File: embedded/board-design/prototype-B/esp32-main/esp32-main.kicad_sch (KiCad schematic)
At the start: 30 parts, among them J1 Conn_ARM_JTAG_SWD_10, J2 Conn_01x08_Socket, J3 Conn_01x08_Socket, Q1 BC817, Q2 BC817, U1 ESP32-WROVER-E, U2 BD48ExxG

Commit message: [prototype-B]
Updated prototype-B README.md. Refactored schematic.

Signed-off-by: Nicolae-Andrei Vasile <vasilenicolaeandrei@gmail.com>
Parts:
- added D1: SMD22WS-TP, Diode_SMD:D_SOD-323_HandSoldering, symbol Device:D_Schottky
- renumbered D1 to D2
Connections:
- net +3V3: now also D1.1 (K); no longer J1.1 (VTref)
- new net: D1.2 (A), J1.1 (VTref)
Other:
- moved on the sheet: R1, R2, R3

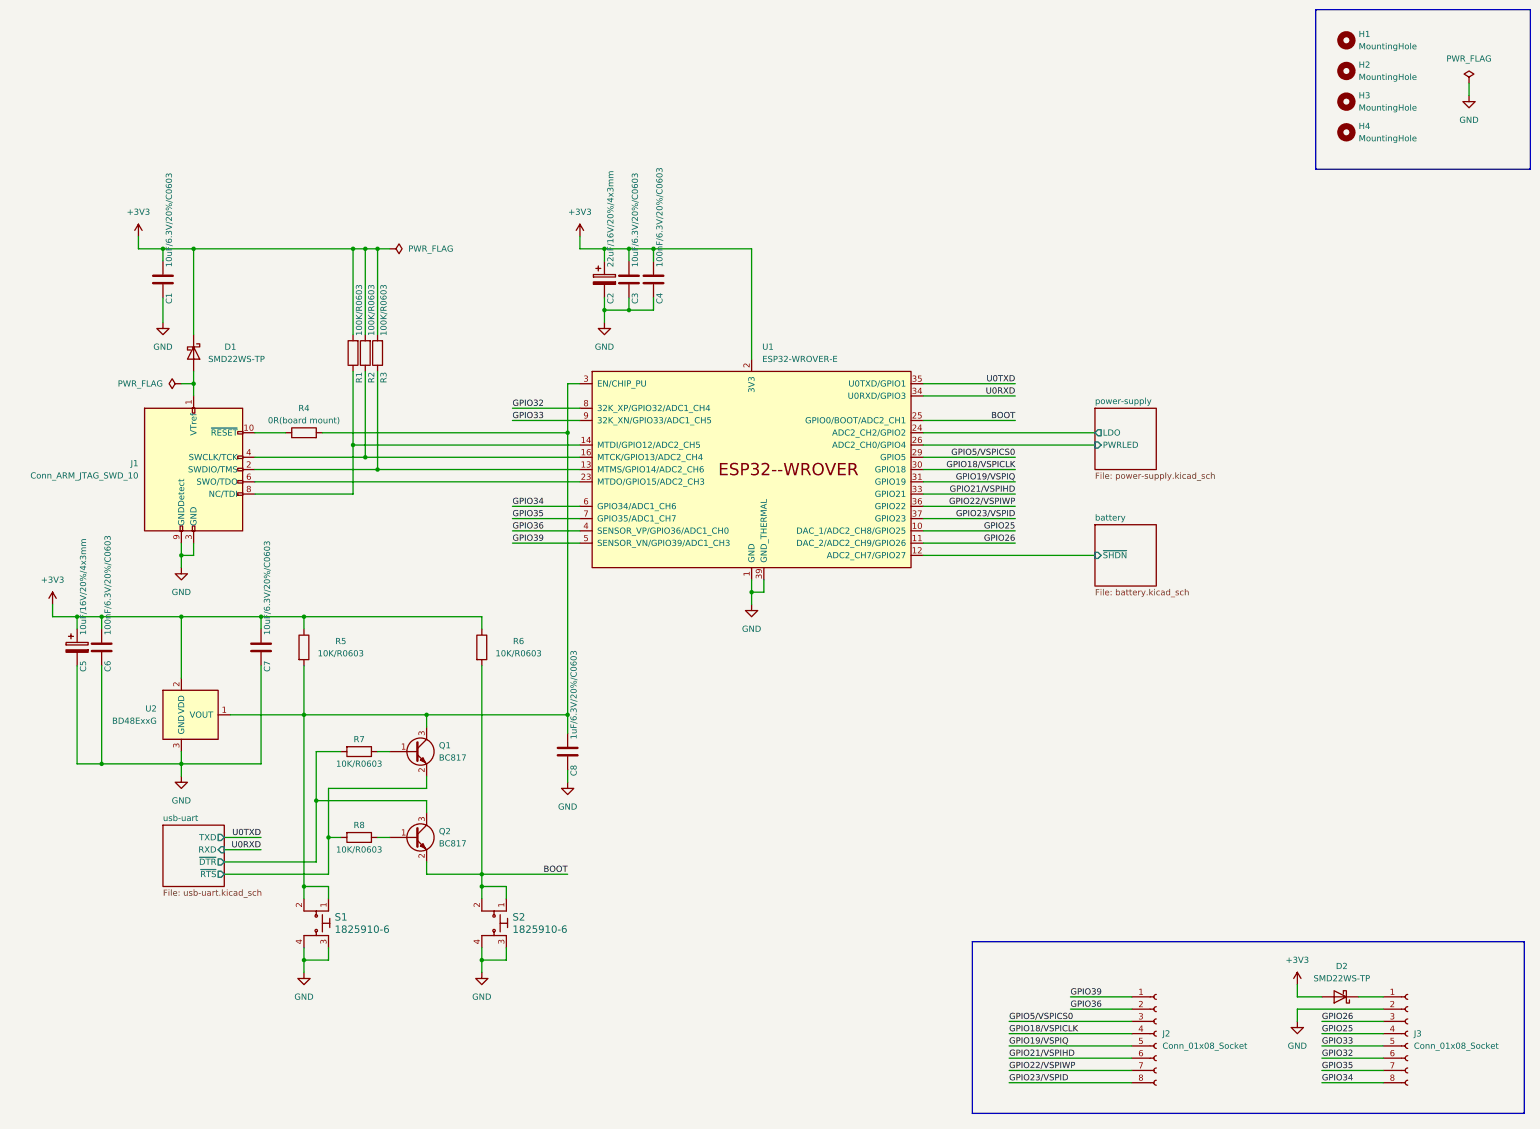
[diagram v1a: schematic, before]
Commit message: [prototype-B]
Refactored hardware implementation.

Signed-off-by: Nicolae-Andrei Vasile <vasilenicolaeandrei@gmail.com>
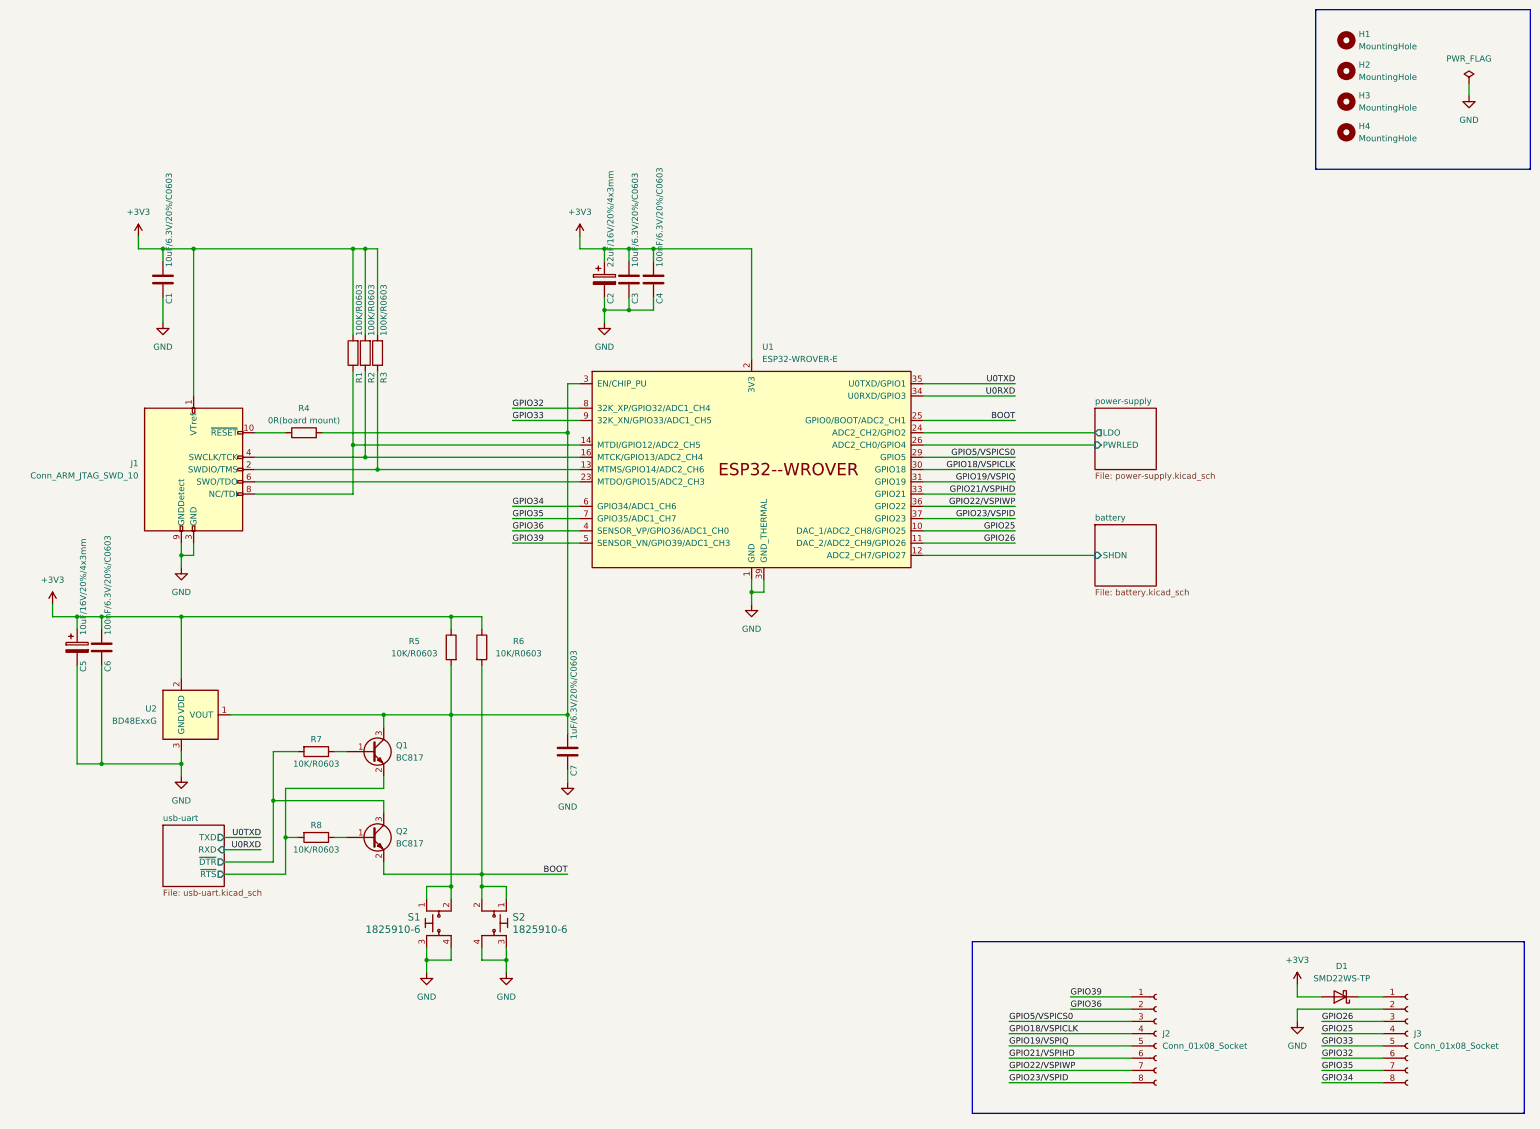
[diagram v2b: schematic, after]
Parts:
- removed C7: 10uF/6.3V/20%/C0603, Capacitor_SMD:C_0603_1608Metric_Pad1.08x0.95mm_HandSolder, symbol Device:C
- removed D1: SMD22WS-TP, Diode_SMD:D_SOD-323_HandSoldering, symbol Device:D_Schottky
- renumbered C8 to C7, D2 to D1
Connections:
- net +3V3: now also J1.1 (VTref)
- net battery/~{SHDN} renamed battery/SHDN
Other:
- sheet battery ports: added SHDN; removed ~{SHDN}
- moved on the sheet: Q1, Q2, R5, R7, R8, S1

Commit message: [prototype-B]
Work in progress - refactoring hardware implementation.

Signed-off-by: Nicolae-Andrei Vasile <vasilenicolaeandrei@gmail.com>
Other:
- note added: "low Vf diode needed"
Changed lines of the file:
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@@
+		)
+	)
+	(text "low Vf diode needed\n"
+		(exclude_from_sim no)
+		(at 342.9 203.2 0)
+		(effects
+			(font
+				(size 1.27 1.27)
+			)
 		)
 	)

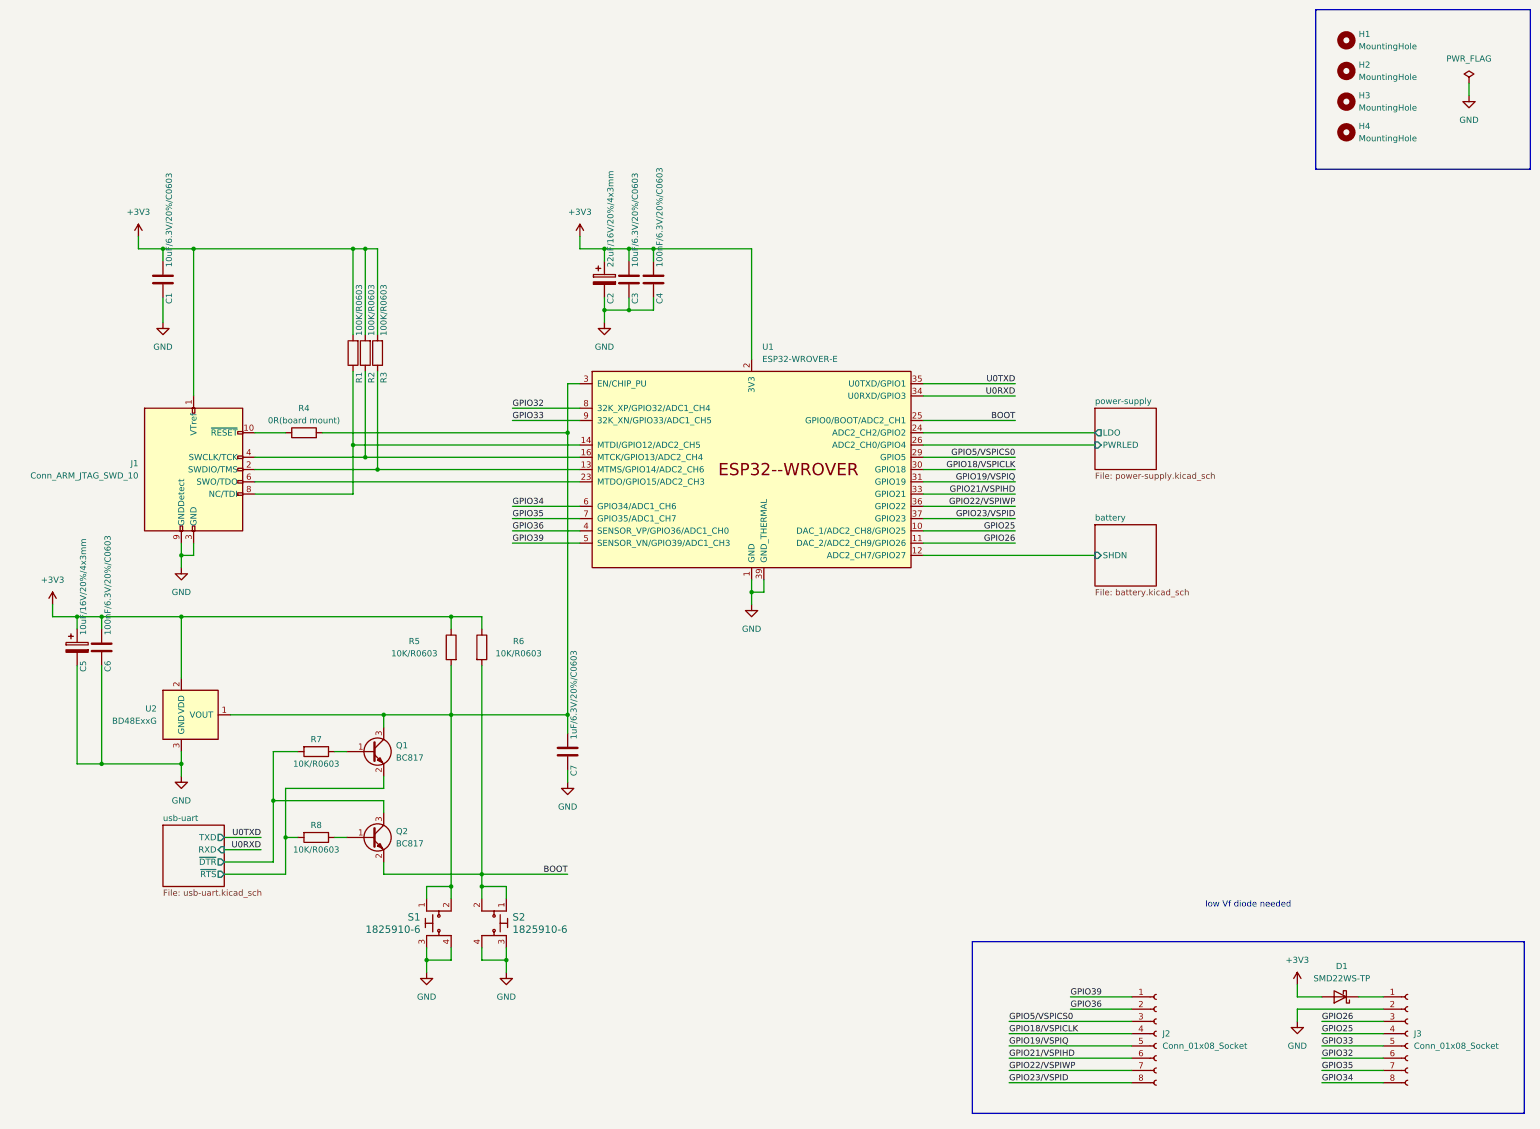
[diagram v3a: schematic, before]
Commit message: [prototype-B]
Refactored hardware implementation. Reduced board size.

Signed-off-by: Nicolae-Andrei Vasile <vasilenicolaeandrei@gmail.com>
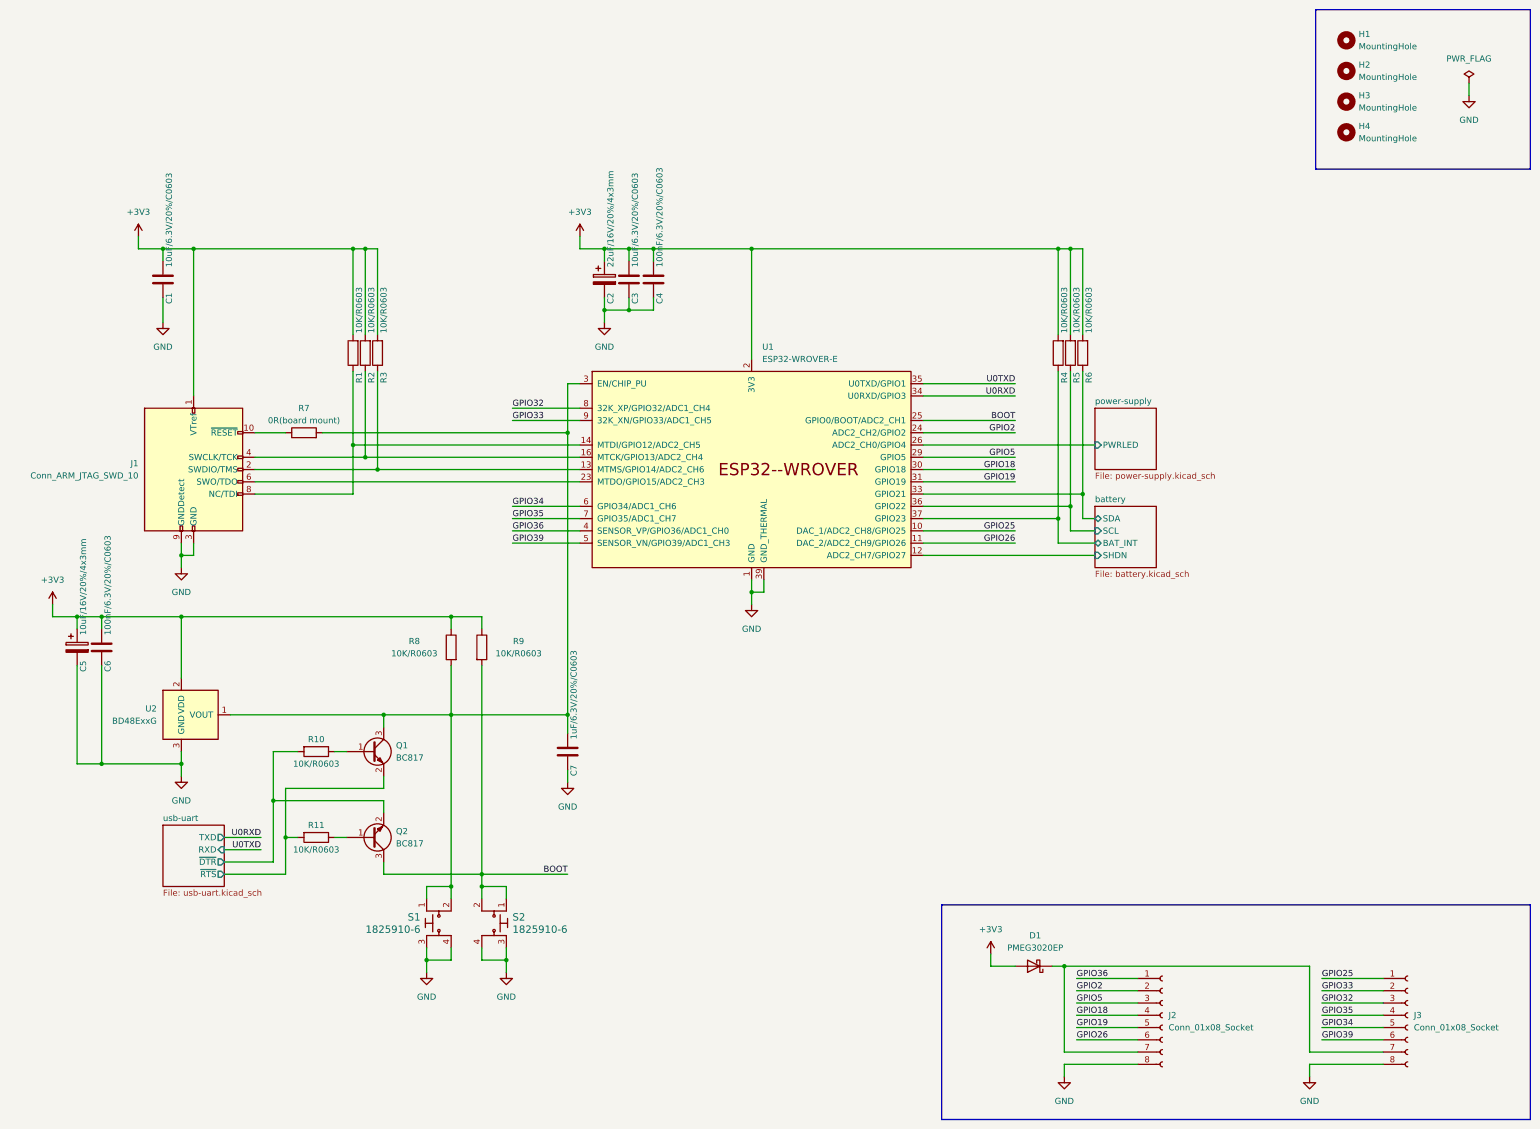
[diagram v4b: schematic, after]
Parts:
- removed D1: SMD22WS-TP, Diode_SMD:D_SOD-323_HandSoldering, symbol Device:D_Schottky
- added D1: PMEG3020EP, Diode_SMD:D_SOD-128, symbol Diode:PMEG3020ER
- added R4, R5, R6: 10K/R0603, Resistor_SMD:R_0603_1608Metric_Pad0.98x0.95mm_HandSolder, symbol Device:R
- J2, J3: footprint Connector_Phoenix_MC:PhoenixContact_MC_1,5_8-G-3.81_1x08_P3.81mm_Horizontal -> TerminalBlock_Phoenix:TerminalBlock_Phoenix_MPT-0,5-8-2.54_1x08_P2.54mm_Horizontal
- R1, R2, R3: value 100K/R0603 -> 10K/R0603
- renumbered R7 to R10, R8 to R11, R4 to R7, R5 to R8, R6 to R9
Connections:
- net +3V3: now also D1.2 (A), R4.2, R5.2, R6.2
- net BOOT: now also Q2.3 (C); no longer Q2.2 (E)
- net GND: now also J2.8 (Pin_8), J3.8 (Pin_8); no longer J3.2 (Pin_2)
- net GPIO25: now also J3.1 (Pin_1); no longer J3.4 (Pin_4)
- net GPIO26: now also J2.6 (Pin_6); no longer J3.3 (Pin_3)
- net GPIO32: now also J3.3 (Pin_3); no longer J3.6 (Pin_6)
- net GPIO33: now also J3.2 (Pin_2); no longer J3.5 (Pin_5)
- net GPIO34: now also J3.5 (Pin_5); no longer J3.8 (Pin_8)
- net GPIO35: now also J3.4 (Pin_4); no longer J3.7 (Pin_7)
- net GPIO36: now also J2.1 (Pin_1); no longer J2.2 (Pin_2)
- net GPIO39: now also J3.6 (Pin_6); no longer J2.1 (Pin_1)
- net usb-uart/~{DTR}: now also Q2.2 (E); no longer Q2.3 (C)
- net GPIO18/VSPICLK renamed GPIO18
- net GPIO19/VSPIQ renamed GPIO19
- net GPIO21/VSPIHD renamed battery/SDA
- net battery/SDA: now also R6.1; no longer J2.6 (Pin_6)
- net GPIO22/VSPIWP: no longer names the net of J2.7 (Pin_7)
- net GPIO22/VSPIWP: now also J3.7 (Pin_7), D1.1 (K); no longer U1.36 (GPIO22)
- net GPIO23/VSPID renamed battery/BAT_INT
- net battery/BAT_INT: now also R4.1; no longer J2.8 (Pin_8)
- net GPIO5/VSPICS0 renamed GPIO5
- net power-supply/LDO renamed GPIO2
- net GPIO2: now also J2.2 (Pin_2)
- new net battery/SCL: R5.1, U1.36 (GPIO22)
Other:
- sheet battery ports: added BAT_INT, SCL, SDA; removed none
- sheet power-supply ports: added none; removed LDO
- note removed: "low Vf diode needed"
